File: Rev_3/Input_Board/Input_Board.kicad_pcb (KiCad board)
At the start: 2 copper layers, 28.5 x 59 mm, 6 parts, among them J1 6, J2 6, J3 6, J6 16

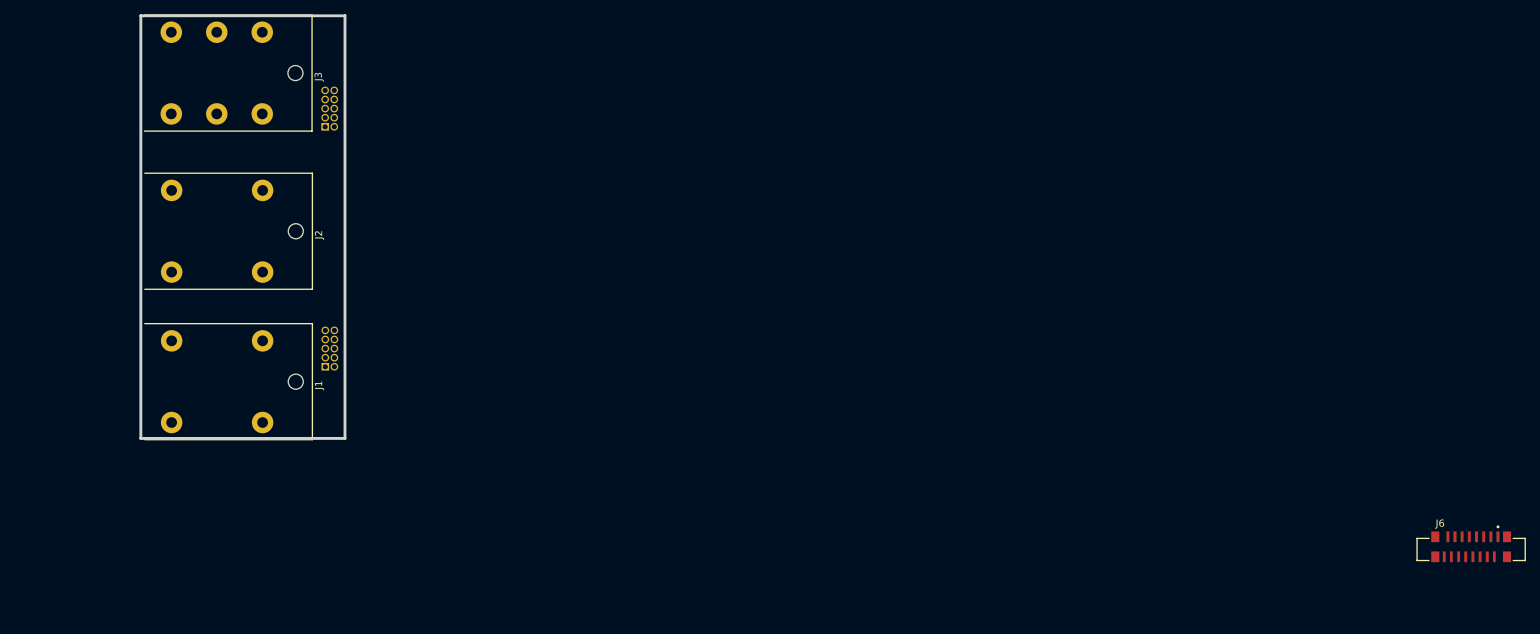
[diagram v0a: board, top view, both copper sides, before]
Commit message: Added analog board back, switched to Jacks on Bottom
Added analog board mezzanine back to fit everything. Finalized decision on jack boards; jacks on bottom, wire to board connectors between jack boards and digital board. Tentative board outlines defined and scoped out component placement.
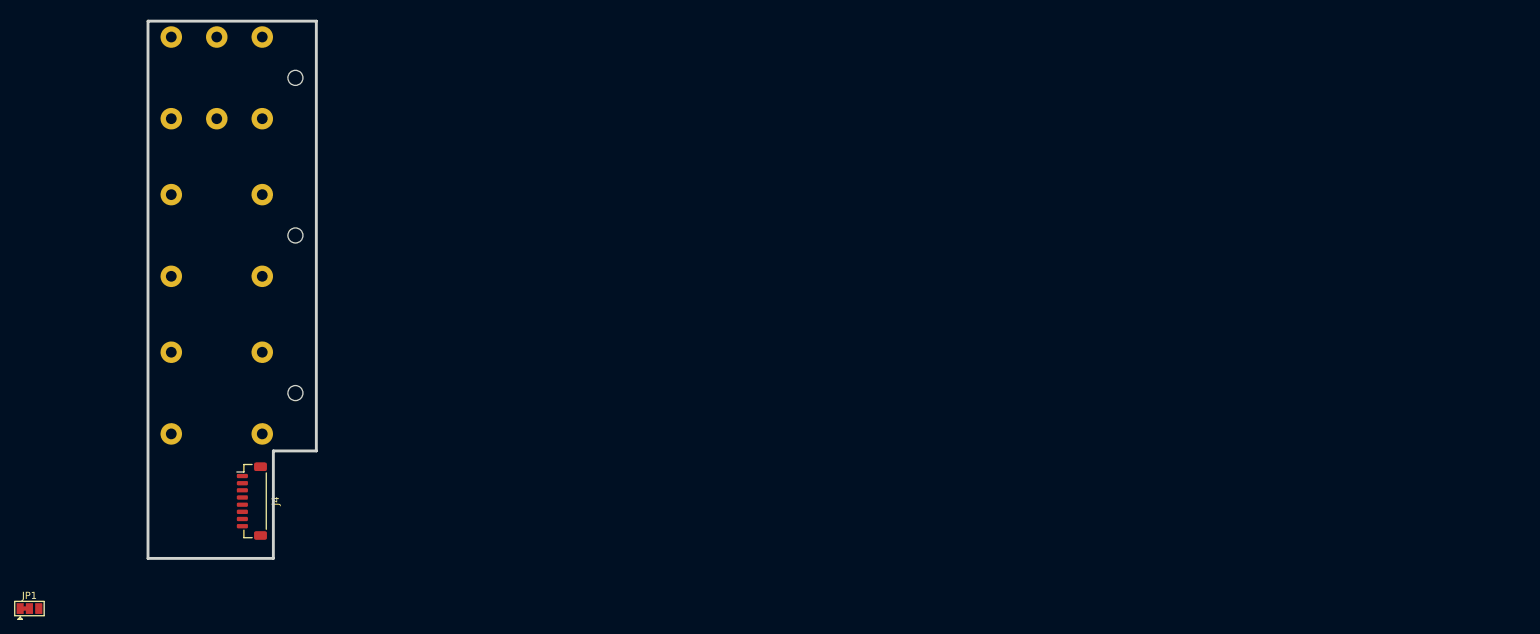
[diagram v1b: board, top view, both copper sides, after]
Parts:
- removed J6: 16, g-con:AMPHENOL_F31W-1A7H1-11016
- removed REF** (x2): CONN_SAMTEC_FTS-105, g-con:CONN_SAMTEC_FTS-105
- added J4: 8, Connector_JST:JST_SH_BM08B-SRSS-TB_1x08-1MP_P1.00mm_Vertical, F.Cu at (86.0, 147.0)
- added JP1: Jumper_3_Bridged12, Jumper:SolderJumper-3_P1.3mm_Bridged12_Pad1.0x1.5mm, F.Cu at (55.0, 162.0)
- J1, J2, J3: moved to B.Cu
- moved J1 1.59 mm to (70.5, 131.9)
- moved J3 0.67 mm to (70.5, 87.9)
- moved J2 0.59 mm to (70.5, 109.9)
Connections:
- J3 pad SN: /r_JACK_SW_EXP -> /JACK_SW_EXP
- J3 pad T: /r_CV_EXP -> /CV_EXP
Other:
- board size 28.5 x 59 mm -> 23.5 x 75 mm
